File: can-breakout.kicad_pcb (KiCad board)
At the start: 2 copper layers, 9 parts, among them J1 Screw_Terminal_01x02, J2 Conn_01x05, J3 Screw_Terminal_01x02, U1 SN65HVD256

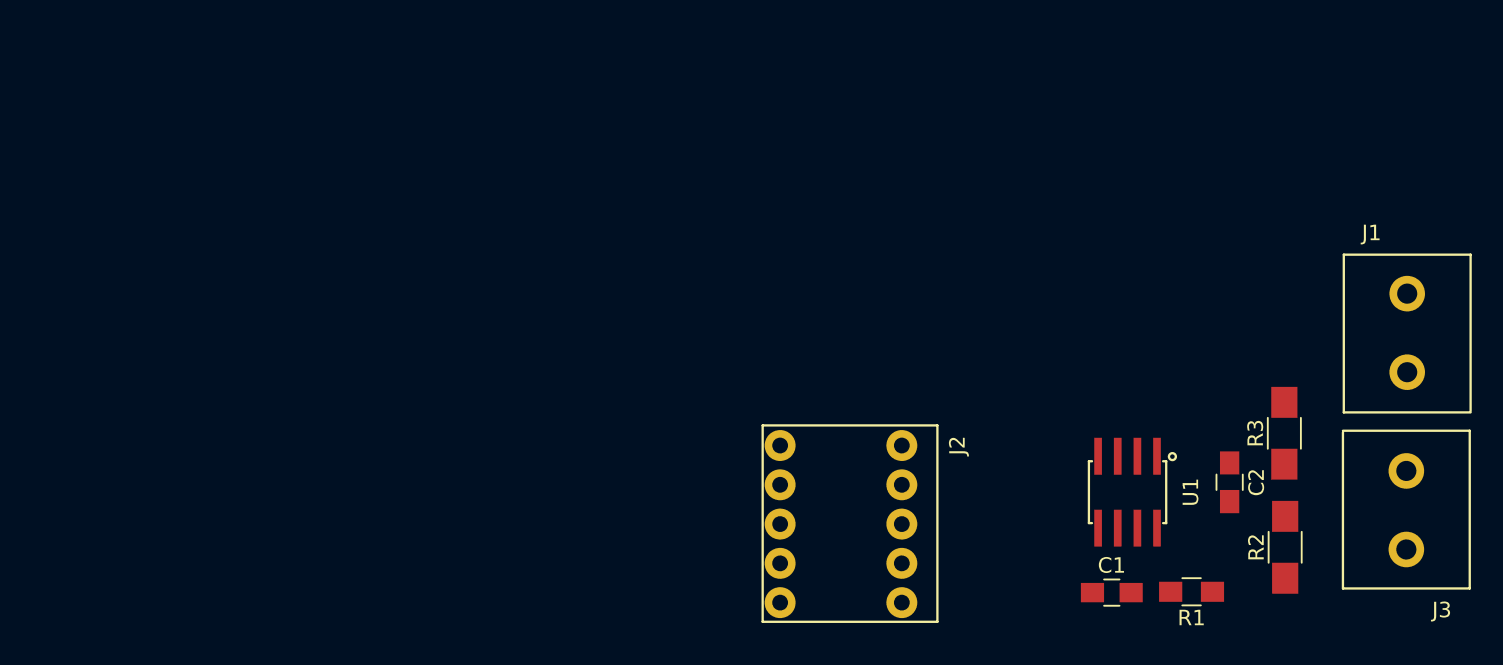
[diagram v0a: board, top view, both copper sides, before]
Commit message: Add vias and ground connections
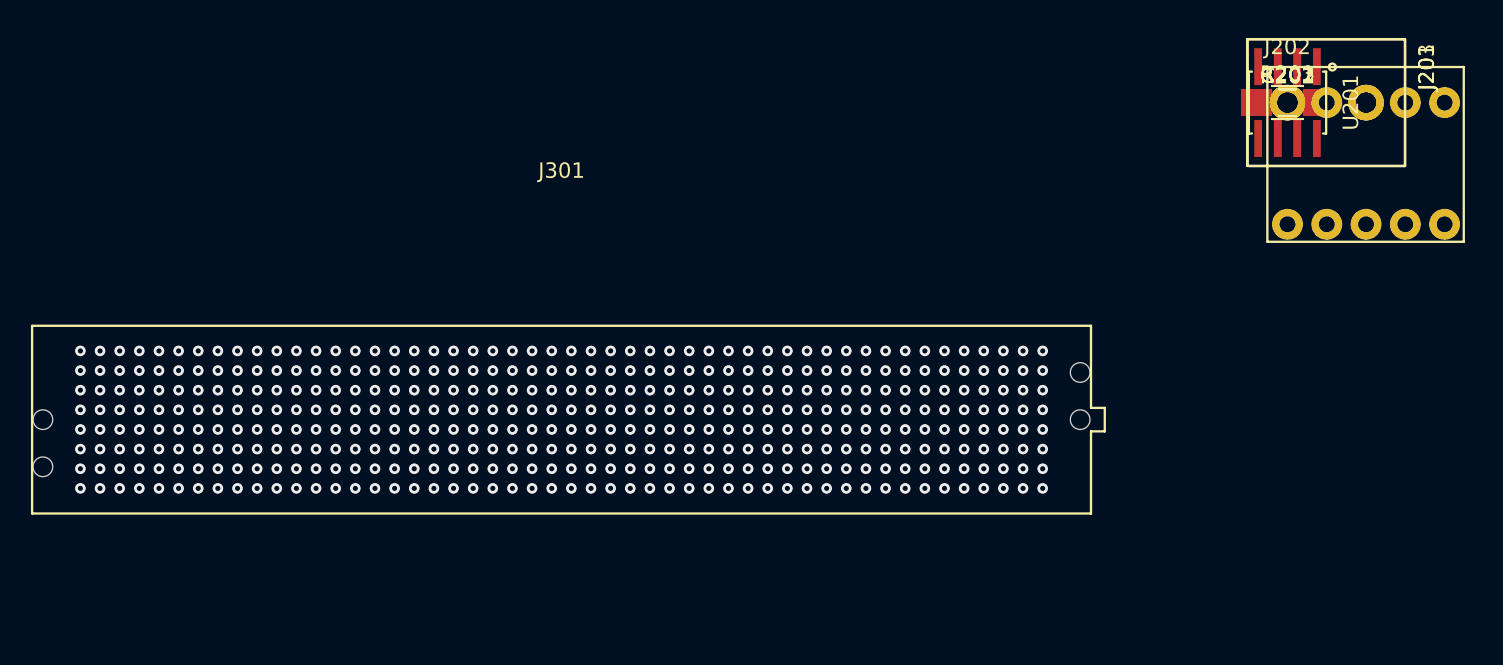
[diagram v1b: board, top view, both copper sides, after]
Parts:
- removed C1: 0u1, Capacitors_SMD:C_0805_HandSoldering
- removed C2: 10n, Capacitors_SMD:C_0805_HandSoldering
- removed J1, J3: Screw_Terminal_01x02, breakout:1729128
- removed J2: Conn_01x05, breakout:M20-7890546
- removed R1: 10k, Resistors_SMD:R_0805_HandSoldering
- removed R2, R3: 60, Resistors_SMD:R_1206_HandSoldering
- removed U1: SN65HVD256, breakout:TI_SOIC8
- added C201: 0u1, Capacitors_SMD:C_0805_HandSoldering, F.Cu at (146.9, 79.5)
- added C202: 10n, Capacitors_SMD:C_0805_HandSoldering, F.Cu at (146.9, 79.5)
- added J201, J203: Screw_Terminal_01x02, breakout:1729128, F.Cu at (146.9, 79.5)
- added J202: Conn_01x05, breakout:M20-7890546, F.Cu at (146.9, 79.5)
- added J301: SEAM-50-02.0-S-08-2-A-K-TR-ND, breakout:SEAM-50-02.0-S-08-2-A-K-TR, F.Cu at (100.0, 100.0)
- added J302: SEAF-50-05.0-S-08-2-A-K-TR, breakout:SEAF-50-05.0-S-08-2-A-K-TR, B.Cu at (100.0, 100.0)
- added R201, R203: 60, Resistors_SMD:R_1206_HandSoldering, F.Cu at (146.9, 79.5)
- added R202: 10k, Resistors_SMD:R_0805_HandSoldering, F.Cu at (146.9, 79.5)
- added U201: SN65HVD256, breakout:TI_SOIC8, F.Cu at (146.9, 79.5)
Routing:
- net Net-(J301-PadH9): vias 0 -> 1
- net Net-(J301-PadH8): vias 0 -> 1
- net Net-(J301-PadH7): vias 0 -> 1
- net Net-(J301-PadH6): vias 0 -> 1
- net Net-(J301-PadH50): vias 0 -> 1
- net Net-(J301-PadH5): vias 0 -> 1
- net Net-(J301-PadH48): vias 0 -> 1
- net Net-(J301-PadH47): vias 0 -> 1
- net Net-(J301-PadH45): vias 0 -> 1
- net Net-(J301-PadH44): vias 0 -> 1
- net Net-(J301-PadH42): vias 0 -> 1
- net Net-(J301-PadH41): vias 0 -> 1
- net Net-(J301-PadH4): vias 0 -> 1
- net Net-(J301-PadH39): vias 0 -> 1
- net Net-(J301-PadH38): vias 0 -> 1
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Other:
- net class Default: clearance 0.2 -> 0.1524; trace_width 0.25 -> 0.1524; via_dia 0.6 -> 0.6858; via_drill 0.4 -> 0.3302
- rule trace_clearance: 0.2 -> 0.1524
- rule trace_min: 0.2 -> 0.1524
- rule via_min_drill: 0.3 -> 0.3302
- rule via_min_size: 0.4 -> 0.6858

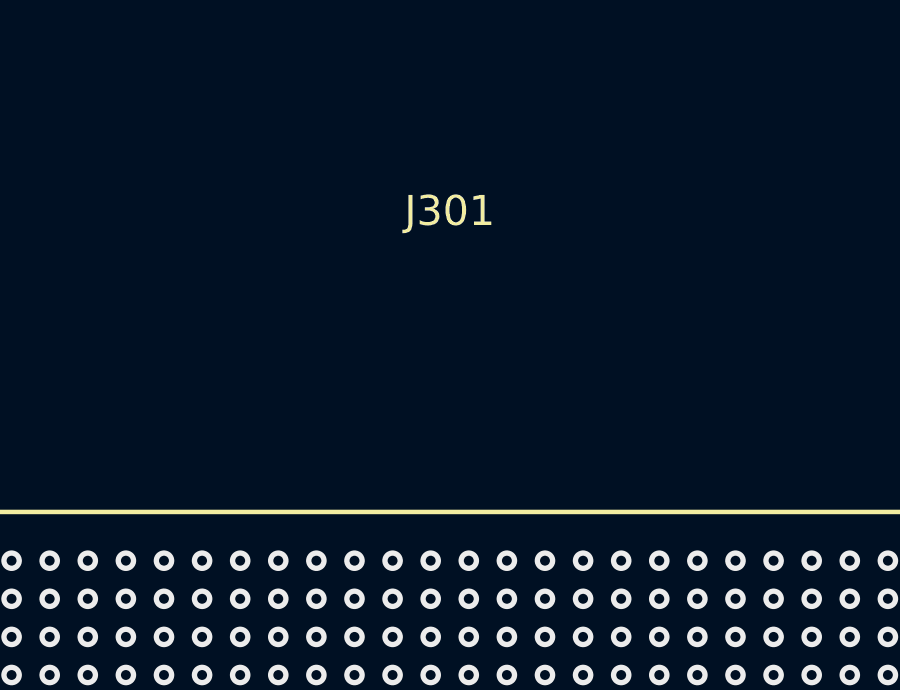
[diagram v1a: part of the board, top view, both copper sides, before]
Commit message: Add hierarchial pins for CAN, TODO regen netlist
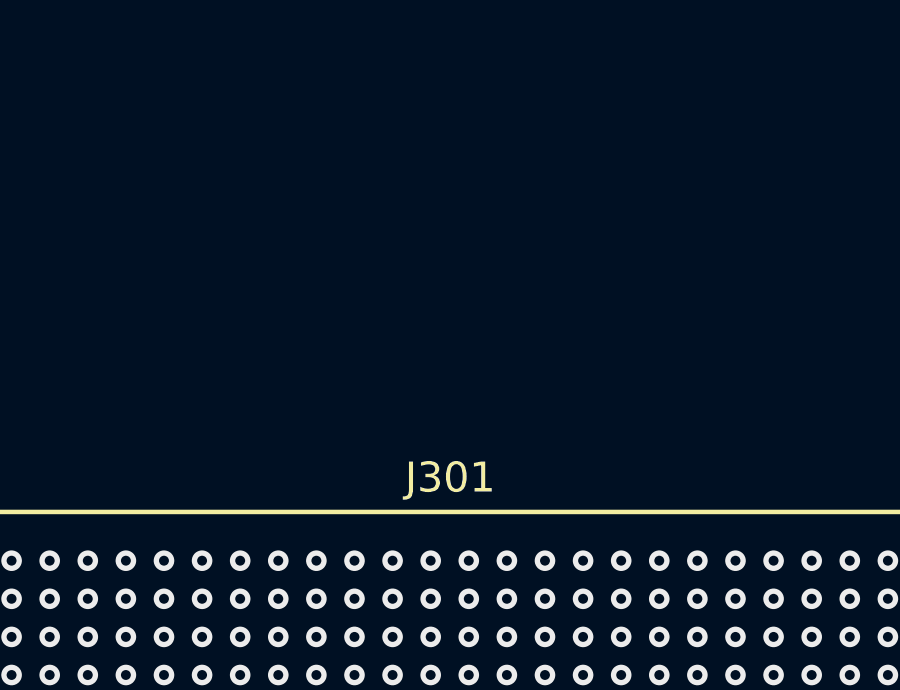
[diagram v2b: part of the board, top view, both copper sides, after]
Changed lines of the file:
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@@
   (module breakout:SEAM-50-02.0-S-08-2-A-K-TR (layer F.Cu)
     (at 100 100)
-    (fp_text reference J301 (at 0 -16.1) (layer F.SilkS)
+    (fp_text reference J301 (at 0.01758 -7.2138) (layer F.SilkS)
       (effects (font (size 1 1) (thickness 0.15)))
     )
-    (fp_text value SEAM-50-02.0-S-08-2-A-K-TR-ND (at 0 -17.7) (layer F.Fab)
+    (fp_text value SEAM-50-02.0-S-08-2-A-K-TR-ND (at -17.30776 -7.33064) (layer F.Fab)
       (effects (font (size 1 1) (thickness 0.15)))
     )
@@
   (module breakout:SEAF-50-05.0-S-08-2-A-K-TR (layer B.Cu)
     (at 100 100)
-    (fp_text reference J302 (at 0 16.1) (layer B.SilkS)
+    (fp_text reference J302 (at -0.03322 7.34548) (layer B.SilkS)
       (effects (font (size 1 1) (thickness 0.15)) (justify mirror))
     )
-    (fp_text value SEAF-50-05.0-S-08-2-A-K-TR (at 0 17.7) (layer B.Fab)
+    (fp_text value SEAF-50-05.0-S-08-2-A-K-TR (at -16.3705 7.59186) (layer B.Fab)
       (effects (font (size 1 1) (thickness 0.15)) (justify mirror))
     )

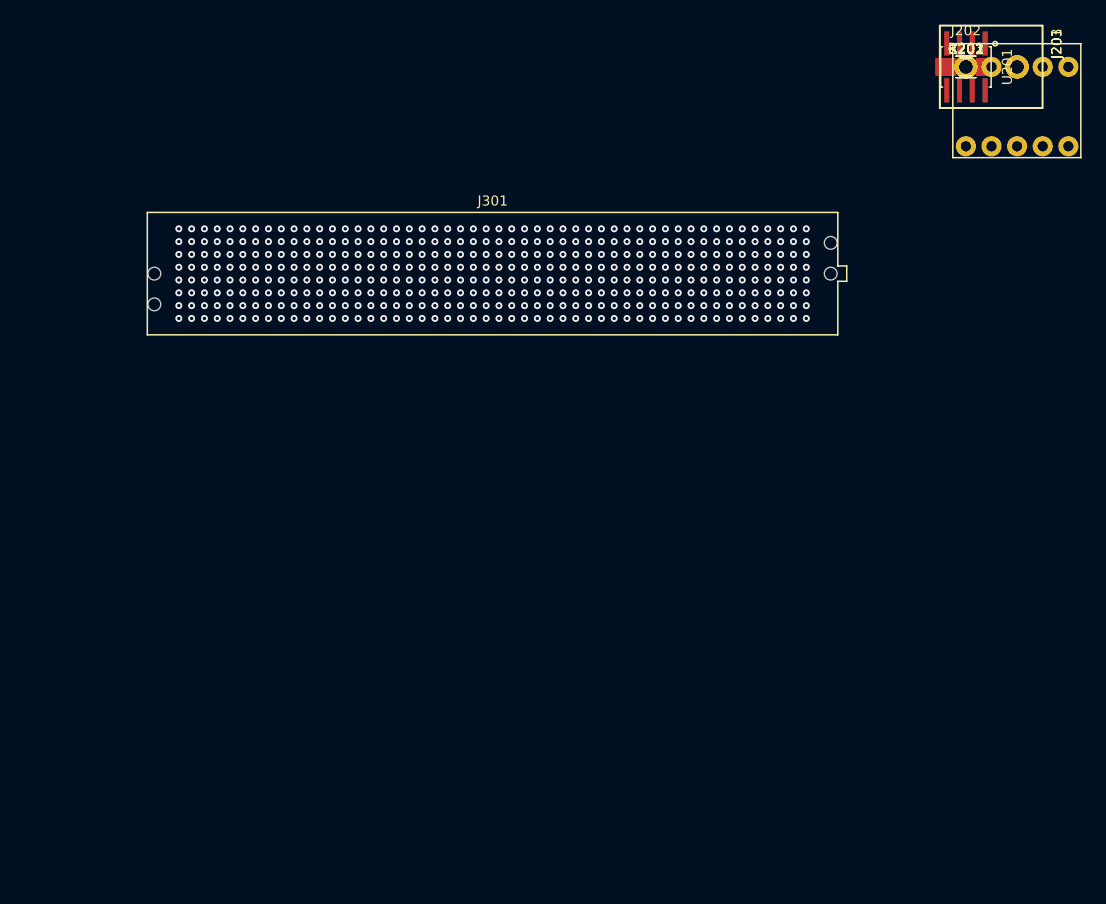
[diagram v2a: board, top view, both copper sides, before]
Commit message: Module outline added to PCB, first CAN bus added
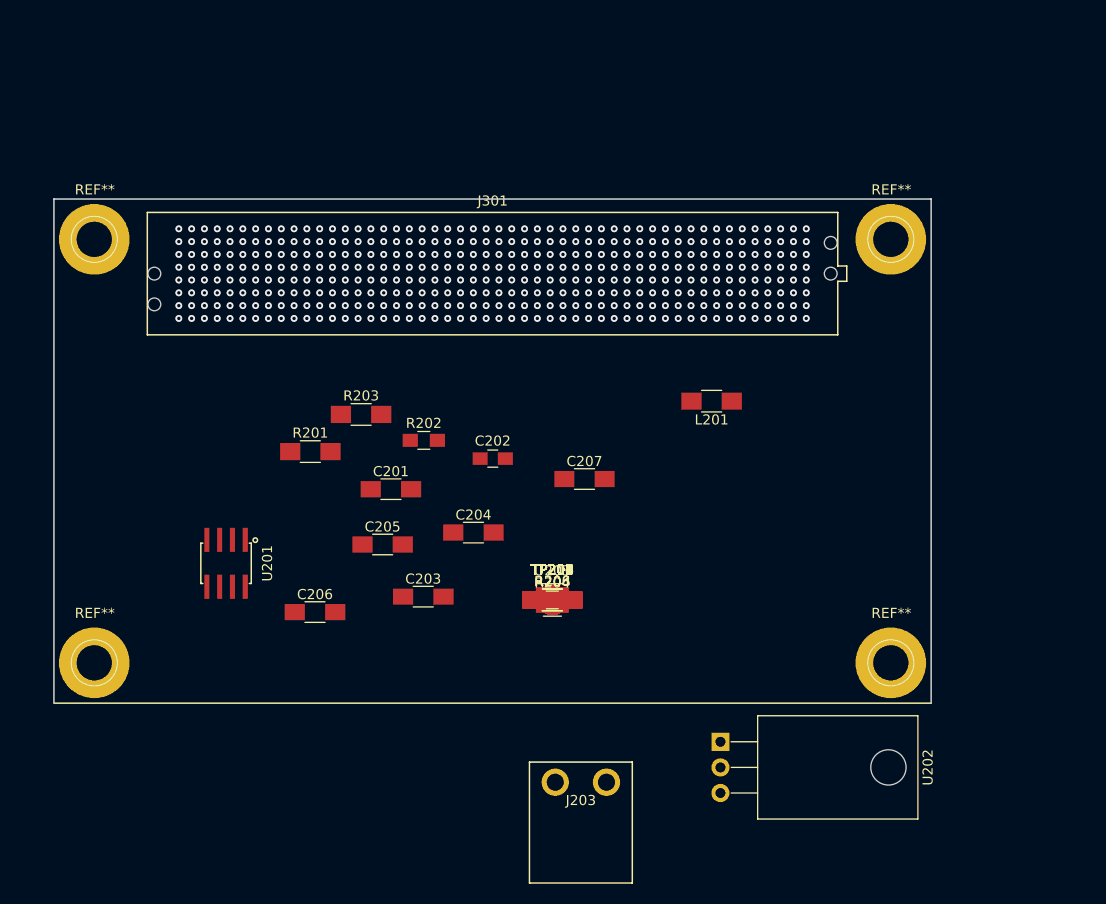
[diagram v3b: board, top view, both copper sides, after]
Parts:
- removed J201: Screw_Terminal_01x02, breakout:1729128
- removed J202: Conn_01x05, breakout:M20-7890546
- added C203: 10u, Capacitors_SMD:C_1206_HandSoldering, F.Cu at (93.1, 132.0)
- added C204: 0u1, Capacitors_SMD:C_1206_HandSoldering, F.Cu at (98.1, 125.7)
- added C205: 10u, Capacitors_SMD:C_1206_HandSoldering, F.Cu at (89.1, 126.9)
- added C206: 10u, Capacitors_SMD:C_1206_HandSoldering, F.Cu at (82.4, 133.6)
- added C207: 0u1, Capacitors_SMD:C_1206_HandSoldering, F.Cu at (109.1, 120.4)
- added L201: Ferrite, Resistors_SMD:R_1206_HandSoldering, F.Cu at (121.7, 112.6)
- added R204: DNC, Resistors_SMD:R_0805_HandSoldering, F.Cu at (105.9, 132.4)
- added R206, R208: 4k7, Resistors_SMD:R_1206_HandSoldering, F.Cu at (105.9, 132.4)
- added REF**: 1pin, Connect:1pin, F.Cu at (60.5, 138.6)
- added REF**: 1pin, Connect:1pin, F.Cu at (139.5, 138.6)
- added REF**: 1pin, Connect:1pin, F.Cu at (139.5, 96.6)
- added REF**: 1pin, Connect:1pin, F.Cu at (60.5, 96.6)
- added TP201, TP202, TP203, TP204, TP205, TP206, TP207, TP208, TP209, TP210: TEST, Measurement_Points:Measurement_Point_Round-SMD-Pad_Big, F.Cu at (105.9, 132.4)
- added U202: LM7805_TO220, TO_SOT_Packages_THT:TO-220-3_Horizontal, F.Cu at (122.6, 146.4)
- added U203: MIC5365-3.3YD5-TR, TO_SOT_Packages_SMD:SOT-23-5, F.Cu at (105.9, 132.4)
- C201: value 0u1 -> 10u; footprint Capacitors_SMD:C_0805_HandSoldering -> Capacitors_SMD:C_1206_HandSoldering
- J203: footprint breakout:1729128 -> breakout:39532-0002
- moved U201 88.4 mm to (73.6, 128.7)
- moved J203 80.6 mm to (108.8, 150.4)
- moved R201 75.4 mm to (81.9, 117.7)
- moved C201 70.8 mm to (89.9, 121.4)
- moved R203 69.2 mm to (87.0, 114.0)
- moved R202 65.3 mm to (93.2, 116.5)
- moved C202 60.9 mm to (100.0, 118.3)
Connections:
- net Net-(J301-PadD18) renamed /CONNECTOR/CAN0_TX
- net Net-(J301-PadD19) renamed /CONNECTOR/CAN0_RX
- J301 pad A1: Net-(J301-PadA1) -> /CAN_TRANSCEIVER/VBAT
- J301 pad A2: Net-(J301-PadA2) -> /CAN_TRANSCEIVER/VBAT
- J302 pad A1: Net-(J301-PadA1) -> /CAN_TRANSCEIVER/VBAT
- J302 pad A2: Net-(J301-PadA2) -> /CAN_TRANSCEIVER/VBAT
- U201 pad 3: Net-(J201-Pad1) -> +5V
- U201 pad 5: Net-(C201-Pad1) -> +3V3
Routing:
- net Net-(J301-PadA2): vias 1 -> 0
- net Net-(J301-PadA1): vias 1 -> 0
- net /CAN_TRANSCEIVER/VBAT: vias 0 -> 2
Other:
- board outline added: 87 x 50 mm
